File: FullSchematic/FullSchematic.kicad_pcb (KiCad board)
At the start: 4 copper layers, 155 x 136 mm, 104 parts, among them J1 USB_A, J10 LCD_Conn, J2 ATX-24, J3 Red Banana Jack, J4 Black Banana Jack, J5 2x6 Pin Header, J6 2x6 Pin Header, J7 CT3151-2, J8 CT3151-2, J9 2x6 Pin Header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

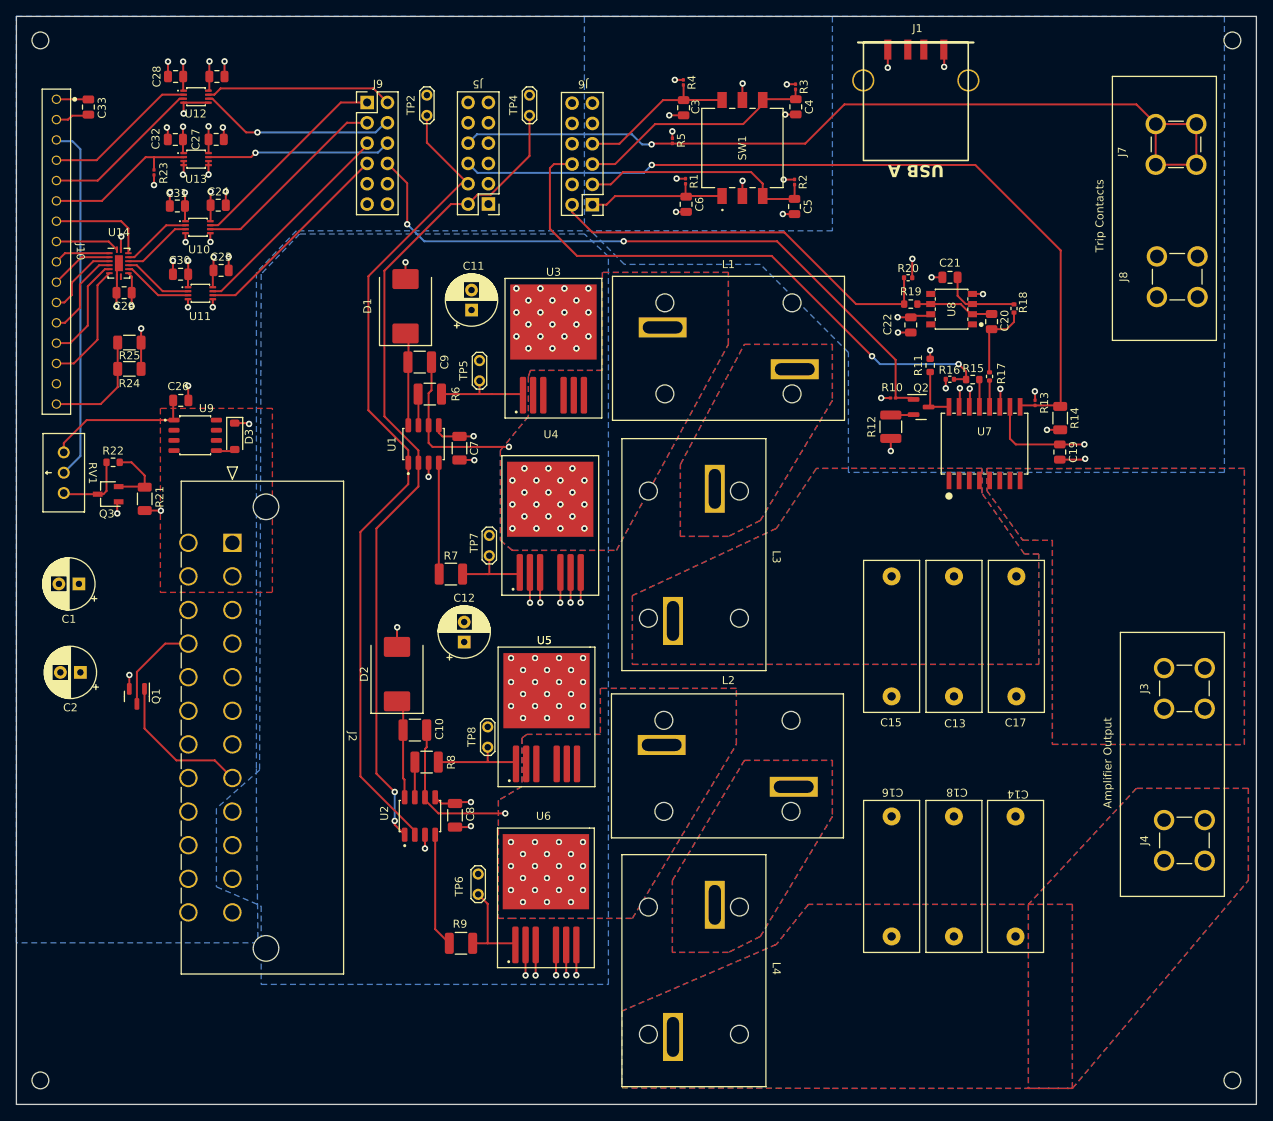
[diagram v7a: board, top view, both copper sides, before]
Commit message: PCB v.3
see teams for full changes
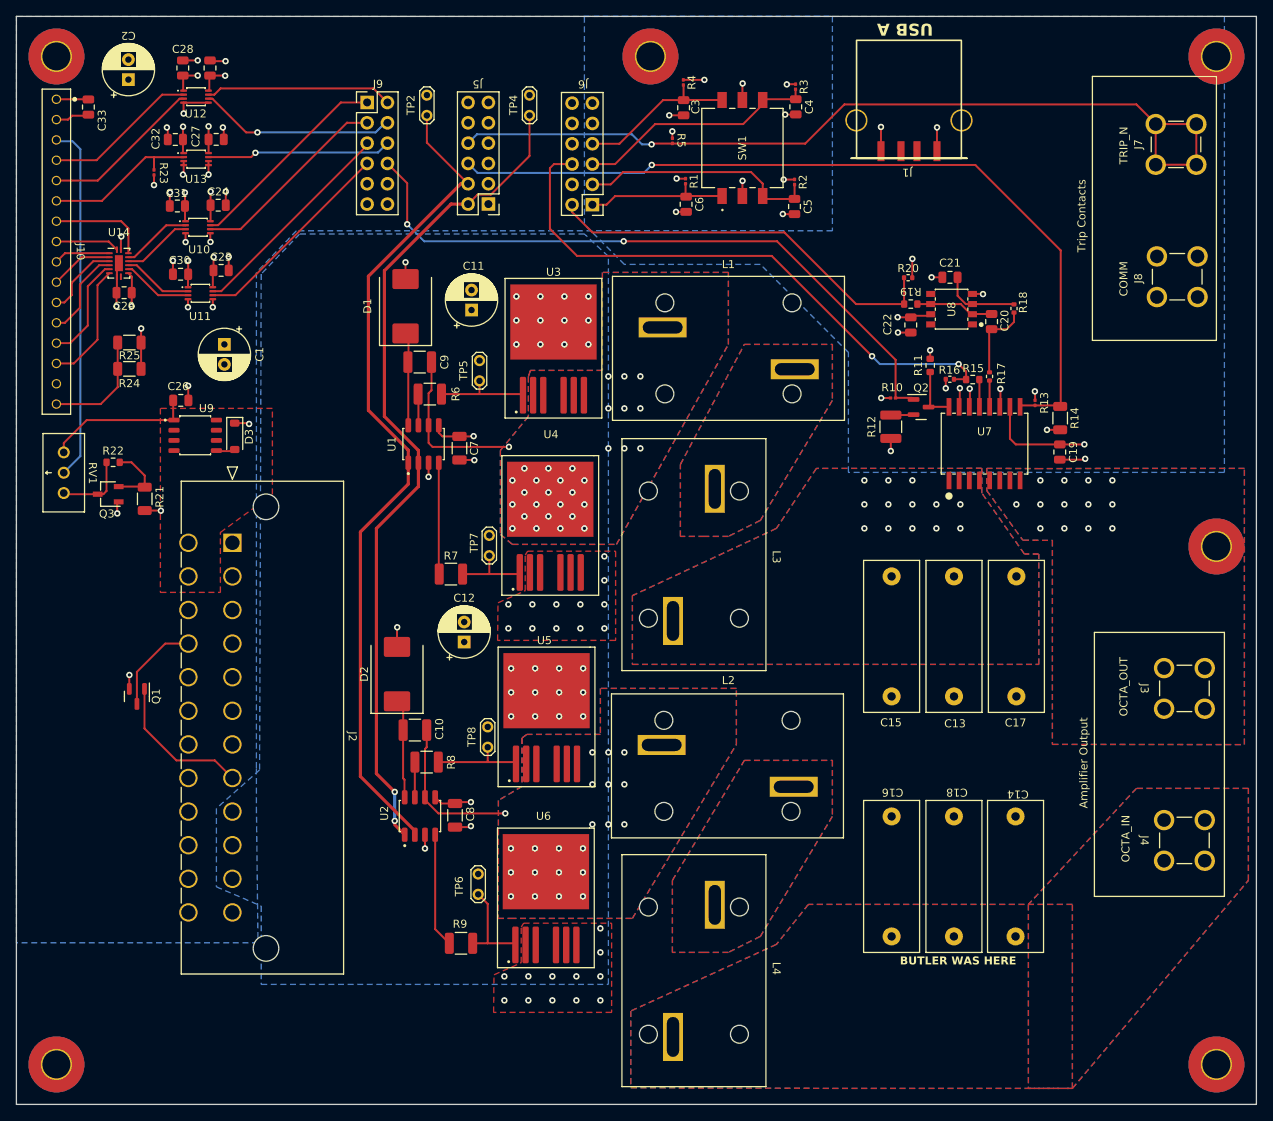
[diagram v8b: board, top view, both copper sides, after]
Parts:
- removed the REF** at (212.0, 27.0)
- removed the REF** at (63.0, 27.0)
- removed the REF** at (212.0, 157.0)
- removed the REF** at (63.0, 157.0)
- added REF**: MountingHole_3.5mm_Pad_TopBottom, MountingHole:MountingHole_3.5mm_Pad_TopBottom, F.Cu at (210.0, 29.0)
- added REF**: MountingHole_3.5mm_Pad_TopBottom, MountingHole:MountingHole_3.5mm_Pad_TopBottom, F.Cu at (139.2, 29.0)
- added REF**: MountingHole_3.5mm_Pad_TopBottom, MountingHole:MountingHole_3.5mm_Pad_TopBottom, F.Cu at (65.0, 155.0)
- added REF**: MountingHole_3.5mm_Pad_TopBottom, MountingHole:MountingHole_3.5mm_Pad_TopBottom, F.Cu at (210.0, 155.0)
- added REF**: MountingHole_3.5mm_Pad_TopBottom, MountingHole:MountingHole_3.5mm_Pad_TopBottom, F.Cu at (65.0, 29.0)
- added REF**: MountingHole_3.5mm_Pad_TopBottom, MountingHole:MountingHole_3.5mm_Pad_TopBottom, F.Cu at (210.0, 90.2)
- moved C2 74.3 mm to (74.0, 31.9), turned to 90 degrees
- moved C1 35.0 mm to (86.0, 65.0), turned to -90 degrees
- moved J1 15.0 mm to (171.6, 27.0), turned to 180 degrees
- moved C28 1.40 mm to (80.8, 30.4), turned to 90 degrees
- moved C25 1.37 mm to (84.2, 30.4), turned to 90 degrees
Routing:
- net COM: track 122.5 -> 85.4 mm, vias 54 -> 68
- net +3.3V: track 20.1 -> 21.7 mm
- net +5V: track 52.3 -> 53.0 mm
- net OCTA_OUT: vias 0 -> 13
- net Net-(U1-VS): vias 22 -> 31
- net AMP_OUT: vias 0 -> 13
- net +12V: vias 46 -> 28
- added copper zone on F.Cu, net COM
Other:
- board text added: "BUTLER WAS HERE"
- board text added: "COMM"
- board text added: "OCTA_IN"
- board text added: "OCTA_OUT"
- board text added: "TRIP_N"
